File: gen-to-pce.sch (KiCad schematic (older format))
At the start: 9 parts

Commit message: First pass at PCB. Needs some work. I don't know what I'm doing, lol
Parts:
- J1: renamed from J?; footprint (none) -> digikey-footprints:DSUB-9_Jack_5747840-3
- J2: renamed from J?; footprint (none) -> w_conn_av:minidin-8
- U1: renamed from U?; value 74LS04 -> 74HC04; footprint (none) -> Package_DIP:DIP-14_W7.62mm_LongPads
- U2: renamed from U?; footprint (none) -> Package_DIP:DIP-14_W7.62mm_LongPads
- U3: renamed from U?; value 74LS157 -> 74HC157; footprint (none) -> Package_DIP:DIP-16_W7.62mm_LongPads
- gave numbers to parts that had none: 1
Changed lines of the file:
@@
 $EndDescr
 $Comp
-L 74xx:74LS157 U?
+L 74xx:74LS157 U3
 U 1 1 5B8C724A
 P 7500 4200
-F 0 "U?" H 7500 5278 50  0000 C CNN
-F 1 "74LS157" H 7500 5187 50  0000 C CNN
-F 2 "" H 7500 4200 50  0001 C CNN
+F 0 "U3" H 7500 5278 50  0000 C CNN
+F 1 "74HC157" H 7500 5187 50  0000 C CNN
+F 2 "Package_DIP:DIP-16_W7.62mm_LongPads" H 7500 4200 50  0001 C CNN
 F 3 "http://www.ti.com/lit/gpn/sn74LS157" H 7500 4200 50  0001 C CNN
 	1    7500 4200
@@
 $EndComp
 $Comp
-L Connector:DB9_Male J?
+L Connector:DB9_Male J1
 U 1 1 5B8C751B
 P 2450 4400
-F 0 "J?" H 2370 3708 50  0000 C CNN
+F 0 "J1" H 2370 3708 50  0000 C CNN
 F 1 "DB9_Male" H 2370 3799 50  0000 C CNN
-F 2 "" H 2450 4400 50  0001 C CNN
+F 2 "digikey-footprints:DSUB-9_Jack_5747840-3" H 2450 4400 50  0001 C CNN
 F 3 " ~" H 2450 4400 50  0001 C CNN
 	1    2450 4400
@@
 $EndComp
 $Comp
-L 74xx:74HC74 U?
+L 74xx:74HC74 U2
 U 1 1 5B8C7BF6
 P 4550 5050
-F 0 "U?" H 4550 5528 50  0000 C CNN
+F 0 "U2" H 4550 5528 50  0000 C CNN
 F 1 "74HC74" H 4550 5437 50  0000 C CNN
-F 2 "" H 4550 5050 50  0001 C CNN
+F 2 "Package_DIP:DIP-14_W7.62mm_LongPads" H 4550 5050 50  0001 C CNN
 F 3 "74xx/74hc_hct74.pdf" H 4550 5050 50  0001 C CNN
 	1    4550 5050
@@
 $EndComp
 $Comp
-L 74xx:74HC74 U?
+L 74xx:74HC74 U2
 U 2 1 5B8C7C6F
 P 6200 5050
-F 0 "U?" H 6200 5528 50  0000 C CNN
+F 0 "U2" H 6200 5528 50  0000 C CNN
 F 1 "74HC74" H 6200 5437 50  0000 C CNN
 F 2 "" H 6200 5050 50  0001 C CNN
@@
 $EndComp
 $Comp
-L 74xx:74HC74 U?
+L 74xx:74HC74 U2
 U 3 1 5B8C7CD8
 P 5150 7000
-F 0 "U?" H 5380 7046 50  0000 L CNN
+F 0 "U2" H 5380 7046 50  0000 L CNN
 F 1 "74HC74" H 5380 6955 50  0000 L CNN
 F 2 "" H 5150 7000 50  0001 C CNN
@@
 $EndComp
 $Comp
-L 74xx:74LS04 U?
+L 74xx:74LS04 U1
 U 1 1 5B8C7E8A
 P 3950 5050
-F 0 "U?" H 3950 5367 50  0000 C CNN
-F 1 "74LS04" H 3950 5276 50  0000 C CNN
-F 2 "" H 3950 5050 50  0001 C CNN
+F 0 "U1" H 3950 5367 50  0000 C CNN
+F 1 "74HC04" H 3950 5276 50  0000 C CNN
+F 2 "Package_DIP:DIP-14_W7.62mm_LongPads" H 3950 5050 50  0001 C CNN
 F 3 "http://www.ti.com/lit/gpn/sn74LS04" H 3950 5050 50  0001 C CNN
 	1    3950 5050
@@
 $EndComp
 $Comp
-L 74xx:74LS04 U?
+L 74xx:74LS04 U1
 U 2 1 5B8C7F8E
 P 5600 5050
-F 0 "U?" H 5600 5367 50  0000 C CNN
-F 1 "74LS04" H 5600 5276 50  0000 C CNN
-F 2 "" H 5600 5050 50  0001 C CNN
+F 0 "U1" H 5600 5367 50  0000 C CNN
+F 1 "74HC04" H 5600 5276 50  0000 C CNN
+F 2 "Package_DIP:DIP-14_W7.62mm_LongPads" H 5600 5050 50  0001 C CNN
 F 3 "http://www.ti.com/lit/gpn/sn74LS04" H 5600 5050 50  0001 C CNN
 	2    5600 5050
@@
 	3250 4500 5900 4500
 $Comp
-L 74xx:74LS04 U?
+L 74xx:74LS04 U1
 U 7 1 5B8D2343
 P 6000 7000
-F 0 "U?" H 6230 7046 50  0000 L CNN
-F 1 "74LS04" H 6230 6955 50  0000 L CNN
-F 2 "" H 6000 7000 50  0001 C CNN
+F 0 "U1" H 6230 7046 50  0000 L CNN
+F 1 "74HC04" H 6230 6955 50  0000 L CNN
+F 2 "Package_DIP:DIP-14_W7.62mm_LongPads" H 6000 7000 50  0001 C CNN
 F 3 "http://www.ti.com/lit/gpn/sn74LS04" H 6000 7000 50  0001 C CNN
 	7    6000 7000
@@
 GND
 $Comp
-L Connector:Conn_01x08_Female J?
+L Connector:Conn_01x08_Female J2
 U 1 1 5B8FEB16
 P 8850 4000
-F 0 "J?" H 8877 3976 50  0000 L CNN
+F 0 "J2" H 8877 3976 50  0000 L CNN
 F 1 "Conn_01x08_Female" H 8877 3885 50  0000 L CNN
-F 2 "" H 8850 4000 50  0001 C CNN
+F 2 "w_conn_av:minidin-8" H 8850 4000 50  0001 C CNN
 F 3 "~" H 8850 4000 50  0001 C CNN
 	1    8850 4000
@@
 GND
 $Comp
+L power:GND #PWR0101
+U 1 1 5B947D21
+P 8650 4400
+F 0 "#PWR0101" H 8650 4150 50  0001 C CNN
+F 1 "GND" H 8655 4227 50  0000 C CNN
+F 2 "" H 8650 4400 50  0001 C CNN
+F 3 "" H 8650 4400 50  0001 C CNN
+	1    8650 4400
+	1    0    0    -1
+$EndComp
+$Comp
+L power:+5V #PWR0102
+U 1 1 5B947DCE
+P 8650 3700
+F 0 "#PWR0102" H 8650 3550 50  0001 C CNN
+F 1 "+5V" H 8665 3873 50  0000 C CNN
+F 2 "" H 8650 3700 50  0001 C CNN
+F 3 "" H 8650 3700 50  0001 C CNN
+	1    8650 3700
+	1    0    0    -1
+$EndComp
+Text GLabel 8650 3700 0    50   Input ~ 0
++5V
+Wire Wire Line
+	4850 4950 4950 4950
+Wire Wire Line
+	4950 4950 4950 3900
+Wire Wire Line
+	6750 4950 6500 4950
+Text GLabel 4550 4750 2    50   Input ~ 0
++5V
+Text GLabel 4550 5350 2    50   Input ~ 0
++5V
+Text GLabel 6200 5350 2    50   Input ~ 0
++5V
+Text GLabel 6200 4750 2    50   Input ~ 0
++5V
+Wire Wire Line
+	4950 3900 7000 3900
+Wire Wire Line
+	6750 4950 6750 3600
+Wire Wire Line
+	6750 3600 7000 3600
+$Comp
 L power:GND #PWR?
-U 1 1 5B947D21
+U 1 1 5B934A3C
 P 8650 4400
 F 0 "#PWR?" H 8650 4150 50  0001 C CNN
@@
 	1    0    0    -1
 $EndComp
+Connection ~ 8650 4400
 $Comp
 L power:+5V #PWR?
-U 1 1 5B947DCE
+U 1 1 5B934BDC
 P 8650 3700
 F 0 "#PWR?" H 8650 3550 50  0001 C CNN
@@
 	1    0    0    -1
 $EndComp
-Text GLabel 8650 3700 0    50   Input ~ 0
-+5V
-Wire Wire Line
-	4850 4950 4950 4950
-Wire Wire Line
-	4950 4950 4950 3900
-Wire Wire Line
-	6750 4950 6500 4950
-Text GLabel 4550 4750 2    50   Input ~ 0
-+5V
-Text GLabel 4550 5350 2    50   Input ~ 0
-+5V
-Text GLabel 6200 5350 2    50   Input ~ 0
-+5V
-Text GLabel 6200 4750 2    50   Input ~ 0
-+5V
-Wire Wire Line
-	4950 3900 7000 3900
-Wire Wire Line
-	6750 4950 6750 3600
-Wire Wire Line
-	6750 3600 7000 3600
+Connection ~ 8650 3700
 $EndSCHEMATC

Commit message: Ground fill, larger power traces, rectanglular edge cuts
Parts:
- added unit 3 of U1
- added unit 4 of U1
- added unit 5 of U1
- added unit 6 of U1
- J2: symbol Connector:Conn_01x08_Female -> Connector_Generic_Shielded:Conn_01x08_Shielded
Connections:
- wire segments 55 -> 61
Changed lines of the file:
@@
 GND
 $Comp
-L Connector:Conn_01x08_Female J2
+L Connector_Generic_Shielded:Conn_01x08_Shielded J2
 U 1 1 5B8FEB16
 P 8850 4000
@@
 F 1 "Conn_01x08_Female" H 8877 3885 50  0000 L CNN
 F 2 "w_conn_av:minidin-8" H 8850 4000 50  0001 C CNN
-F 3 "~" H 8850 4000 50  0001 C CNN
+F 3 "https://www.cui.com/product/resource/digikeypdf/md-sg-series.pdf" H 8850 4000 50  0001 C CNN
 	1    8850 4000
 	1    0    0    -1
@@
 Wire Wire Line
 	6950 5300 8350 5300
-Text GLabel 8650 4400 0    50   Input ~ 0
+Text GLabel 8650 4600 0    50   Input ~ 0
 GND
 $Comp
 L power:GND #PWR0101
 U 1 1 5B947D21
-P 8650 4400
-F 0 "#PWR0101" H 8650 4150 50  0001 C CNN
-F 1 "GND" H 8655 4227 50  0000 C CNN
-F 2 "" H 8650 4400 50  0001 C CNN
-F 3 "" H 8650 4400 50  0001 C CNN
-	1    8650 4400
+P 8650 4600
+F 0 "#PWR0101" H 8650 4350 50  0001 C CNN
+F 1 "GND" H 8655 4427 50  0000 C CNN
+F 2 "" H 8650 4600 50  0001 C CNN
+F 3 "" H 8650 4600 50  0001 C CNN
+	1    8650 4600
 	1    0    0    -1
 $EndComp
@@
 	6750 3600 7000 3600
 $Comp
-L power:GND #PWR?
-U 1 1 5B934A3C
-P 8650 4400
-F 0 "#PWR?" H 8650 4150 50  0001 C CNN
-F 1 "GND" H 8655 4227 50  0000 C CNN
-F 2 "" H 8650 4400 50  0001 C CNN
-F 3 "" H 8650 4400 50  0001 C CNN
-	1    8650 4400
-	1    0    0    -1
-$EndComp
-Connection ~ 8650 4400
-$Comp
-L power:+5V #PWR?
+L power:+5V #PWR0104
 U 1 1 5B934BDC
 P 8650 3700
-F 0 "#PWR?" H 8650 3550 50  0001 C CNN
+F 0 "#PWR0104" H 8650 3550 50  0001 C CNN
 F 1 "+5V" H 8665 3873 50  0000 C CNN
 F 2 "" H 8650 3700 50  0001 C CNN
@@
 $EndComp
 Connection ~ 8650 3700
+$Comp
+L 74xx:74HC04 U1
+U 3 1 5B968A1B
+P 2450 6150
+F 0 "U1" H 2600 6400 50  0000 C CNN
+F 1 "74HC04" H 2650 6300 50  0000 C CNN
+F 2 "" H 2450 6150 50  0001 C CNN
+F 3 "http://www.nxp.com/documents/data_sheet/74HC_HCT04.pdf" H 2450 6150 50  0001 C CNN
+	3    2450 6150
+	1    0    0    -1
+$EndComp
+$Comp
+L 74xx:74HC04 U1
+U 4 1 5B968A9D
+P 2450 6500
+F 0 "U1" H 2600 6700 50  0000 C CNN
+F 1 "74HC04" H 2650 6600 50  0000 C CNN
+F 2 "" H 2450 6500 50  0001 C CNN
+F 3 "http://www.nxp.com/documents/data_sheet/74HC_HCT04.pdf" H 2450 6500 50  0001 C CNN
+	4    2450 6500
+	1    0    0    -1
+$EndComp
+$Comp
+L 74xx:74HC04 U1
+U 5 1 5B968B21
+P 2450 6850
+F 0 "U1" H 2600 7100 50  0000 C CNN
+F 1 "74HC04" H 2650 7000 50  0000 C CNN
+F 2 "" H 2450 6850 50  0001 C CNN
+F 3 "http://www.nxp.com/documents/data_sheet/74HC_HCT04.pdf" H 2450 6850 50  0001 C CNN
+	5    2450 6850
+	1    0    0    -1
+$EndComp
+$Comp
+L 74xx:74HC04 U1
+U 6 1 5B968BA2
+P 2450 7200
+F 0 "U1" H 2600 7400 50  0000 C CNN
+F 1 "74HC04" H 2650 7300 50  0000 C CNN
+F 2 "" H 2450 7200 50  0001 C CNN
+F 3 "http://www.nxp.com/documents/data_sheet/74HC_HCT04.pdf" H 2450 7200 50  0001 C CNN
+	6    2450 7200
+	1    0    0    -1
+$EndComp
+Wire Wire Line
+	2150 6150 2150 6500
+Connection ~ 2150 6500
+Wire Wire Line
+	2150 6500 2150 6850
+Connection ~ 2150 6850
+Wire Wire Line
+	2150 6850 2150 7200
+Connection ~ 2150 7200
+Wire Wire Line
+	2150 7200 2150 7400
+$Comp
+L power:GND #PWR0105
+U 1 1 5B96A6DC
+P 2150 7400
+F 0 "#PWR0105" H 2150 7150 50  0001 C CNN
+F 1 "GND" H 2155 7227 50  0000 C CNN
+F 2 "" H 2150 7400 50  0001 C CNN
+F 3 "" H 2150 7400 50  0001 C CNN
+	1    2150 7400
+	1    0    0    -1
+$EndComp
+Wire Wire Line
+	8650 4400 8650 4600
+Wire Wire Line
+	8650 4600 8850 4600
+Connection ~ 8650 4600
 $EndSCHEMATC

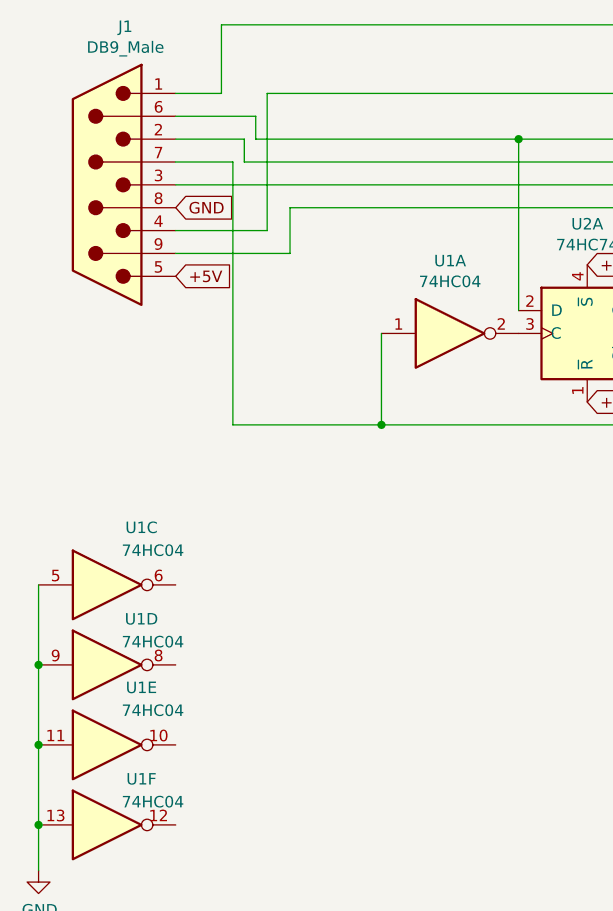
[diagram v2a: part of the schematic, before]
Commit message: M-din-8 mount holes plated, select line delay
Added select line delay for genesis controller to make sure there's no
problem with propagation delay and setup time.
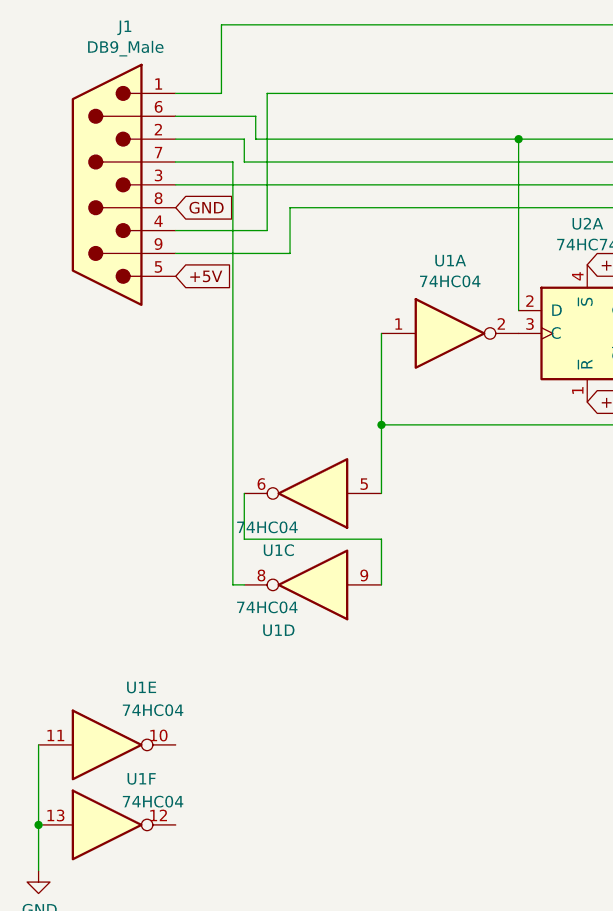
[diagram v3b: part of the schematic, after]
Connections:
- wire segments 61 -> 63
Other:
- moved on the sheet: U1C, U1D
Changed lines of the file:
@@
 	5300 5450 3650 5450
 Wire Wire Line
-	3650 5450 3000 5450
-Wire Wire Line
-	3000 5450 3000 4300
-Wire Wire Line
 	3000 4300 2750 4300
-Connection ~ 3650 5450
 Text GLabel 2750 4800 2    50   Input ~ 0
 +5V
@@
 L 74xx:74HC04 U1
 U 3 1 5B968A1B
-P 2450 6150
-F 0 "U1" H 2600 6400 50  0000 C CNN
-F 1 "74HC04" H 2650 6300 50  0000 C CNN
-F 2 "" H 2450 6150 50  0001 C CNN
-F 3 "http://www.nxp.com/documents/data_sheet/74HC_HCT04.pdf" H 2450 6150 50  0001 C CNN
-	3    2450 6150
-	1    0    0    -1
+P 3350 5750
+F 0 "U1" H 3500 6000 50  0000 C CNN
+F 1 "74HC04" H 3550 5900 50  0000 C CNN
+F 2 "" H 3350 5750 50  0001 C CNN
+F 3 "http://www.nxp.com/documents/data_sheet/74HC_HCT04.pdf" H 3350 5750 50  0001 C CNN
+	3    3350 5750
+	-1   0    0    1
 $EndComp
 $Comp
 L 74xx:74HC04 U1
 U 4 1 5B968A9D
-P 2450 6500
-F 0 "U1" H 2600 6700 50  0000 C CNN
-F 1 "74HC04" H 2650 6600 50  0000 C CNN
-F 2 "" H 2450 6500 50  0001 C CNN
-F 3 "http://www.nxp.com/documents/data_sheet/74HC_HCT04.pdf" H 2450 6500 50  0001 C CNN
-	4    2450 6500
-	1    0    0    -1
+P 3350 6150
+F 0 "U1" H 3500 6350 50  0000 C CNN
+F 1 "74HC04" H 3550 6250 50  0000 C CNN
+F 2 "" H 3350 6150 50  0001 C CNN
+F 3 "http://www.nxp.com/documents/data_sheet/74HC_HCT04.pdf" H 3350 6150 50  0001 C CNN
+	4    3350 6150
+	-1   0    0    1
 $EndComp
 $Comp
@@
 $EndComp
 Wire Wire Line
-	2150 6150 2150 6500
-Connection ~ 2150 6500
-Wire Wire Line
-	2150 6500 2150 6850
-Connection ~ 2150 6850
-Wire Wire Line
 	2150 6850 2150 7200
 Connection ~ 2150 7200
@@
 	8650 4600 8850 4600
 Connection ~ 8650 4600
+Wire Wire Line
+	3050 5750 3050 5950
+Wire Wire Line
+	3050 5950 3650 5950
+Wire Wire Line
+	3650 5950 3650 6150
+Wire Wire Line
+	3650 5450 3650 5750
+Connection ~ 3650 5450
+Wire Wire Line
+	3000 6150 3050 6150
+Wire Wire Line
+	3000 4300 3000 6150
 $EndSCHEMATC

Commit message: Add DPDT switch, reroute to account for switch
The switch swaps the A button and Start button, which makes it the same
as an Avenue Pad 3, basically. With the Avenue Pad 3, the extra button
exists where the A button is on the Genesis, and the mapping is selected
by a switch on the controller. Some games use III mapped to Sel, some
use III mapped to Run.

The original design had A (which you can consider III) hard-mapped to
Sel. Now it is selectable, which increases compatibility with games that
mapped III to Run instead.
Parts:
- added SW1: SW_DPDT_x2, Button_Switch_THT:SW_E-Switch_EG2219_DPDT_Angled, symbol Switch:SW_DPDT_x2
- J1: value DB9_Male -> DB9 (M)
- J2: value Conn_01x08_Female -> M-DIN-8 (F)
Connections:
- wire segments 63 -> 78
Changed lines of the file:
@@
 P 2450 4400
 F 0 "J1" H 2370 3708 50  0000 C CNN
-F 1 "DB9_Male" H 2370 3799 50  0000 C CNN
+F 1 "DB9 (M)" H 2370 3799 50  0000 C CNN
 F 2 "digikey-footprints:DSUB-9_Jack_5747840-3" H 2450 4400 50  0001 C CNN
 F 3 " ~" H 2450 4400 50  0001 C CNN
@@
 	3250 4700 3250 4500
 Wire Wire Line
-	3250 4500 5900 4500
+	3250 4500 4000 4500
 $Comp
 L 74xx:74LS04 U1
@@
 Wire Wire Line
 	4250 4950 4250 4200
-Connection ~ 4250 4200
-Wire Wire Line
-	4250 4200 7000 4200
 Wire Wire Line
 	5900 4950 5900 4500
-Connection ~ 5900 4500
-Wire Wire Line
-	5900 4500 7000 4500
 Wire Wire Line
 	6850 5450 5300 5450
@@
 U 1 1 5B8FEB16
 P 8850 4000
-F 0 "J2" H 8877 3976 50  0000 L CNN
-F 1 "Conn_01x08_Female" H 8877 3885 50  0000 L CNN
+F 0 "J2" H 8950 4000 50  0000 L CNN
+F 1 "M-DIN-8 (F)" H 8950 3900 50  0000 L CNN
 F 2 "w_conn_av:minidin-8" H 8850 4000 50  0001 C CNN
 F 3 "https://www.cui.com/product/resource/digikeypdf/md-sg-series.pdf" H 8850 4000 50  0001 C CNN
@@
 Wire Wire Line
 	3000 4300 3000 6150
+$Comp
+L Switch:SW_DPDT_x2 SW1
+U 2 1 5B9F6787
+P 4750 3400
+F 0 "SW1" H 4750 3685 50  0000 C CNN
+F 1 "SW_DPDT_x2" H 4750 3594 50  0000 C CNN
+F 2 "Button_Switch_THT:SW_E-Switch_EG2219_DPDT_Angled" H 4750 3400 50  0001 C CNN
+F 3 "" H 4750 3400 50  0001 C CNN
+	2    4750 3400
+	1    0    0    -1
+$EndComp
+$Comp
+L Switch:SW_DPDT_x2 SW1
+U 1 1 5B9F6808
+P 4750 2800
+F 0 "SW1" H 4750 3085 50  0000 C CNN
+F 1 "SW_DPDT_x2" H 4750 2994 50  0000 C CNN
+F 2 "Button_Switch_THT:SW_E-Switch_EG2219_DPDT_Angled" H 4750 2800 50  0001 C CNN
+F 3 "" H 4750 2800 50  0001 C CNN
+	1    4750 2800
+	1    0    0    -1
+$EndComp
+Wire Wire Line
+	6450 3300 6450 4200
+Wire Wire Line
+	6450 4200 7000 4200
+Wire Wire Line
+	7000 4500 6300 4500
+Wire Wire Line
+	4950 3500 5300 3500
+Wire Wire Line
+	6300 3500 6300 4500
+Wire Wire Line
+	4950 3300 5100 3300
+Wire Wire Line
+	4000 4500 4000 2800
+Wire Wire Line
+	4000 2800 4550 2800
+Connection ~ 4000 4500
+Wire Wire Line
+	4000 4500 5900 4500
+Wire Wire Line
+	4250 4200 4250 3400
+Wire Wire Line
+	4250 3400 4550 3400
+Connection ~ 4250 4200
+Wire Wire Line
+	4950 2700 5300 2700
+Wire Wire Line
+	5300 2700 5300 3500
+Connection ~ 5300 3500
+Wire Wire Line
+	5300 3500 6300 3500
+Wire Wire Line
+	4950 2900 5100 2900
+Wire Wire Line
+	5100 2900 5100 3300
+Connection ~ 5100 3300
+Wire Wire Line
+	5100 3300 6450 3300
 $EndSCHEMATC

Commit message: Update to v2.1, wider +5V traces, added decoupling cap
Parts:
- added C1: 10uF, Capacitor_THT:CP_Radial_D5.0mm_P2.50mm, symbol Device:CP
- U3: symbol 74xx:74LS157 -> gen-to-pce-rescue:74LS157-74xx
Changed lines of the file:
@@
 EESchema Schematic File Version 4
 LIBS:gen-to-pce-cache
-EELAYER 26 0
+EELAYER 29 0
 EELAYER END
 $Descr A4 11693 8268
@@
 Sheet 1 1
 Title "Genesis 3-button to PC-Engine adapter"
-Date "2018-09-06"
-Rev "0.2"
+Date "2019-03-31"
+Rev "2.1"
 Comp "Bradon Kanyid"
-Comment1 ""
+Comment1 "https://github.com/rattboi/gen-to-pce-controller-adapter"
 Comment2 ""
 Comment3 ""
@@
 $EndDescr
 $Comp
-L 74xx:74LS157 U3
+L gen-to-pce-rescue:74LS157-74xx U3
 U 1 1 5B8C724A
 P 7500 4200
@@
 Wire Wire Line
 	5100 3300 6450 3300
+$Comp
+L Device:CP C1
+U 1 1 5CA117F7
+P 8950 5100
+F 0 "C1" H 9068 5146 50  0000 L CNN
+F 1 "10uF" H 9068 5055 50  0000 L CNN
+F 2 "Capacitor_THT:CP_Radial_D5.0mm_P2.50mm" H 8988 4950 50  0001 C CNN
+F 3 "~" H 8950 5100 50  0001 C CNN
+	1    8950 5100
+	1    0    0    -1
+$EndComp
+$Comp
+L power:GND #PWR0103
+U 1 1 5CA121B8
+P 8950 5250
+F 0 "#PWR0103" H 8950 5000 50  0001 C CNN
+F 1 "GND" H 8955 5077 50  0000 C CNN
+F 2 "" H 8950 5250 50  0001 C CNN
+F 3 "" H 8950 5250 50  0001 C CNN
+	1    8950 5250
+	1    0    0    -1
+$EndComp
+$Comp
+L power:+5V #PWR0106
+U 1 1 5CA12A3B
+P 8950 4950
+F 0 "#PWR0106" H 8950 4800 50  0001 C CNN
+F 1 "+5V" H 8965 5123 50  0000 C CNN
+F 2 "" H 8950 4950 50  0001 C CNN
+F 3 "" H 8950 4950 50  0001 C CNN
+	1    8950 4950
+	1    0    0    -1
+$EndComp
 $EndSCHEMATC
